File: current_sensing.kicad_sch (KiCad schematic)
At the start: 0 parts

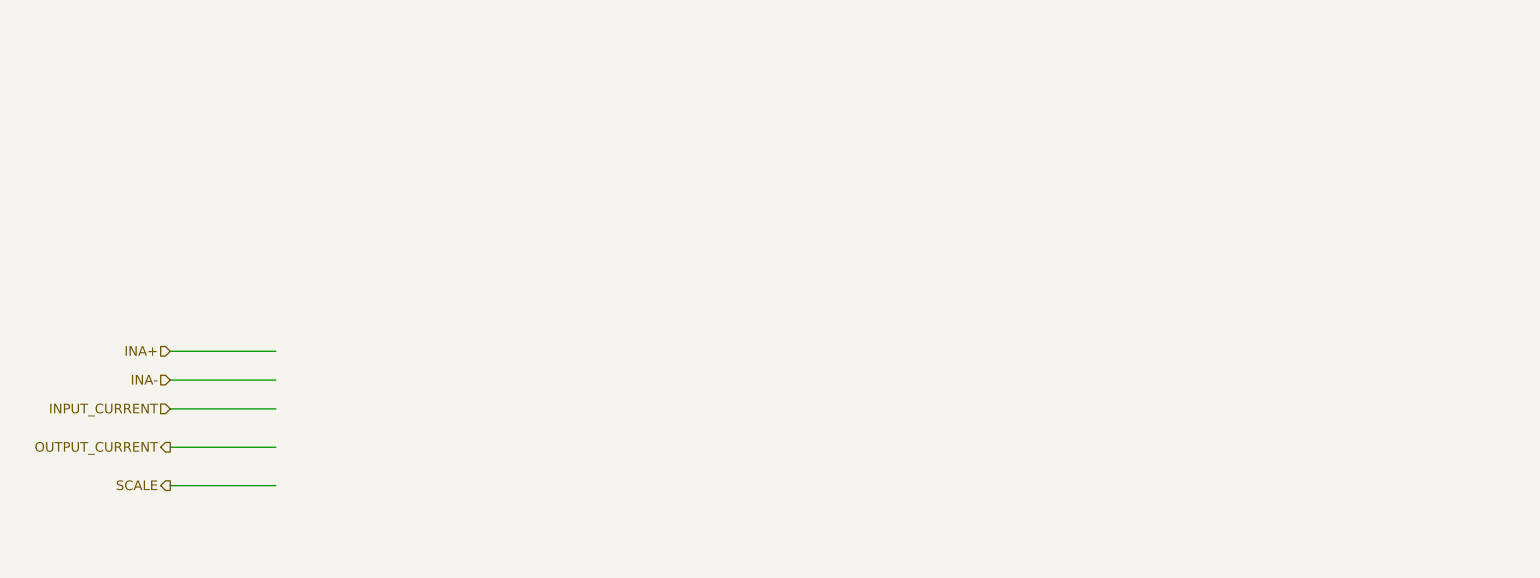
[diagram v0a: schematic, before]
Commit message: HW-61/chore: Added simulation for switch ocntrol, organized the overall schematic, fixed the ERC errors. Still pending for the current sense components and negative side LDO control
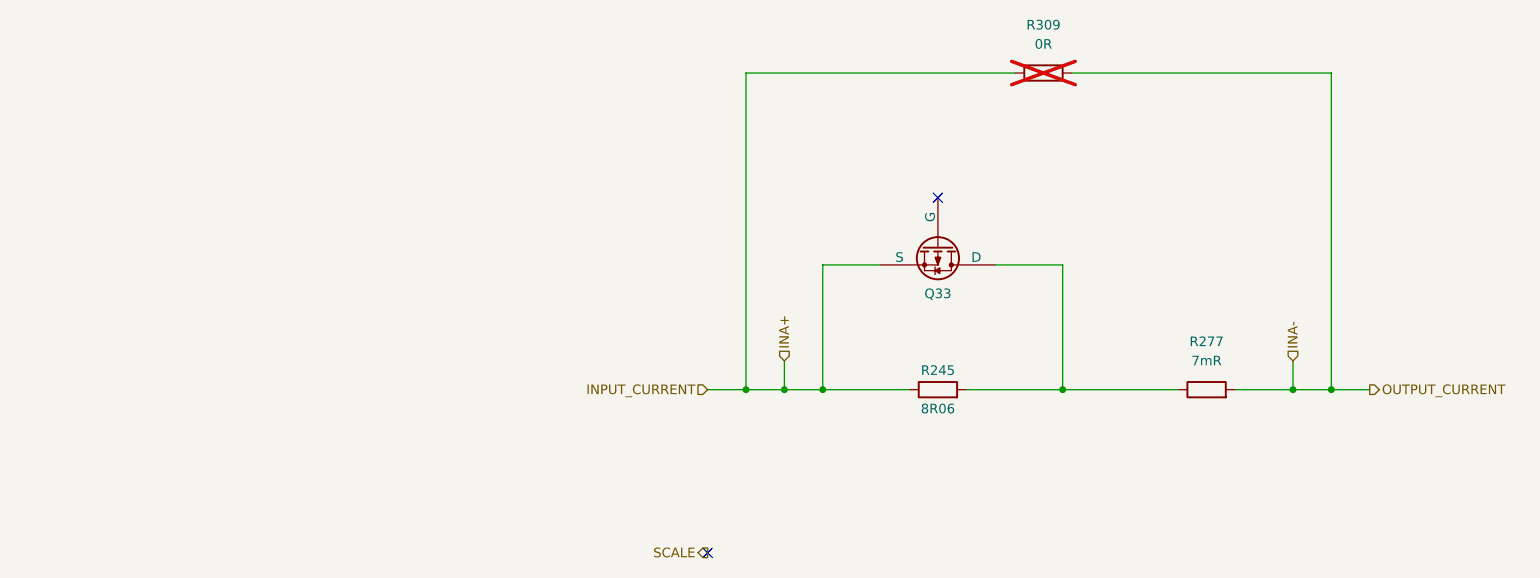
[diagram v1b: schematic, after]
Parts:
- added Q33: SISH625DN-T1-GE3, staging:PowerPAK-8_P0.66_3.3x3.3x0.9, symbol staging:SISH625DN-T1-GE3
- added R245: 8.06R-0805, passive:Resistor_0805, symbol staging:8R06-0805
- added R277: 7mR-0805, passive:Resistor_0805, symbol staging:7mR-0805
- added R309: 0R-0805_01, passive:Resistor_0805, symbol staging:0R-0805
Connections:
- net INA+: now also Q33.1 (S), Q33.2 (S), Q33.3 (S), R245.1, R309.1
- net INA-: now also R277.2, R309.2
- new net: Q33.5 (D), Q33.6 (D), Q33.7 (D), Q33.8 (D), R245.2, R277.1
- no-connect marks 0 -> 2
